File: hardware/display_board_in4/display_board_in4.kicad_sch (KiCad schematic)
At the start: 142 parts, among them J1 Conn_02x05_Odd_Even, J3 Conn_02x05_Odd_Even, Q1 MMBTA42, Q10 MMBTA42, Q11 MMBTA42, Q12 MMBTA42, Q13 MMBTA42, Q14 MMBTA42, Q15 MMBTA42, Q16 MMBTA42, Q17 MMBTA42, Q18 MMBTA42, Q19 MMBTA42, Q2 MMBTA42, Q20 MMBTA42, Q21 MMBTA42, Q22 MMBTA42, Q23 MMBTA42, Q24 MMBTA42, Q25 MMBTA42, Q26 MMBTA42, Q27 MMBTA42, Q28 MMBTA42, Q29 MMBTA42, Q3 MMBTA42, Q30 MMBTA42, Q31 MMBTA42, Q32 MMBTA42, Q33 MMBTA42, Q34 MMBTA42, Q35 MMBTA42, Q36 MMBTA42, Q37 MMBTA42, Q38 MMBTA42, Q39 MMBTA42, Q4 MMBTA42, Q40 MMBTA42, Q41 MMBTA42, Q42 MMBTA42, Q43 MMBTA42, Q44 MMBTA42, Q45 MMBTA42, Q46 MMBTA42, Q47 MMBTA42, Q48 MMBTA42, Q49 MMBTA42, Q5 MMBTA42, Q50 MMBTA42, Q51 MMBTA42, Q52 MMBTA42, Q53 MMBTA42, Q54 MMBTA42, Q55 MMBTA42, Q56 MMBTA42, Q57 MMBTA42, Q58 MMBTA42, Q59 MMBTA42, Q6 MMBTA42, Q60 MMBTA42, Q7 MMBTA42, Q8 MMBTA42, Q9 MMBTA42, SW1 XKB5858-W-E-75, U1 PCA9685PW, U2 PCA9685PW, U3 PCA9685PW, U4 PCA9685PW, U5 LTR-303ALS-01

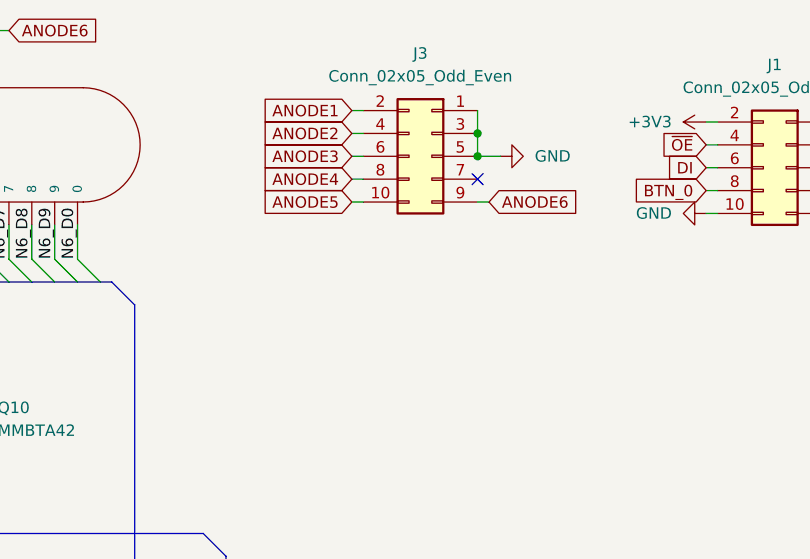
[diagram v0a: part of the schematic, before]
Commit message: hardware(sch): add button and display board identification pin
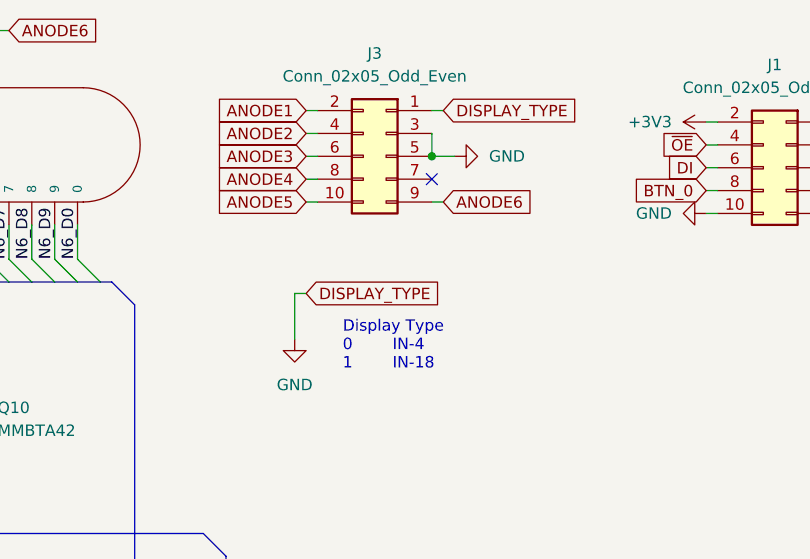
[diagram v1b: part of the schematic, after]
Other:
- note added: "Display Type 0 IN-4 1 IN-18"
- moved on the sheet: J3

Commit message: WIP: pcb layout
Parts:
- R1, R2: now not fitted
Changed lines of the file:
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@@
 		(in_bom no)
 		(on_board yes)
-		(dnp no)
+		(dnp yes)
 		(property "Reference" "R2"
 			(at 31.75 31.75 90)
@@
 		(in_bom no)
 		(on_board yes)
-		(dnp no)
+		(dnp yes)
 		(property "Reference" "R1"
 			(at 29.21 31.75 90)

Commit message: WIP: schematic and layout
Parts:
- removed SW1: XKB5858-W-E-75, habonroof_kicad_library:XKB5858, symbol Johnson_Symbol_Lib:SW_push_RightAngle
- added R64: 0, Resistor_SMD:R_0603_1608Metric, symbol Device:R_Small
- R63: value 10k -> 0; footprint Resistor_SMD:R_0402_1005Metric -> Resistor_SMD:R_0603_1608Metric; LCSC PN C25744 -> (none)
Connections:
- net BTN_0 is gone; now on net GND: J1.8 (Pin_8), R63.2
- net +3V3: now also R64.1; no longer R63.1
- net GND: no longer J3.1 (Pin_1), J3.5 (Pin_5)
- new net DISPLAY_TYPE: J3.1 (Pin_1), R63.1, R64.2
- no-connect marks 8 -> 7
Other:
- note added: "Display Type (analog read) 0V IN-4 1.65V IN14(8pcs) 3.3V IN-14"
- note removed: "Display Type 0 IN-4 1 IN-18"
